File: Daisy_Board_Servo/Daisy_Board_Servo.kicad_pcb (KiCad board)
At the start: 2 copper layers, 29.8 x 46.2 mm, 69 parts, among them IC1 PCA9685PW, IC2 TJA1050T_CM, IC3 LSM6DS3TR-C, IC4 ACS712ELCTR-05B-T, J1 SM04B-SRSS-TB, J10 Conn_01x03_Pin, J11 Conn_01x03_Pin, J12 Conn_01x03_Pin, J13 Conn_01x03_Pin, J14 Conn_01x03_Pin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

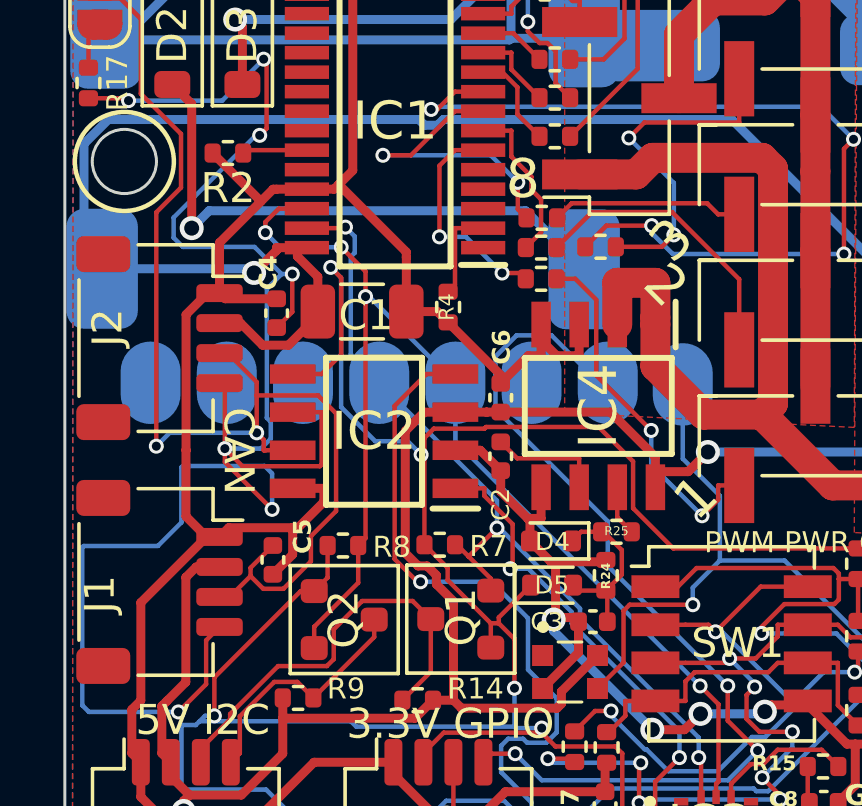
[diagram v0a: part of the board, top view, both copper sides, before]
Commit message: panel updates for lower QTY parts
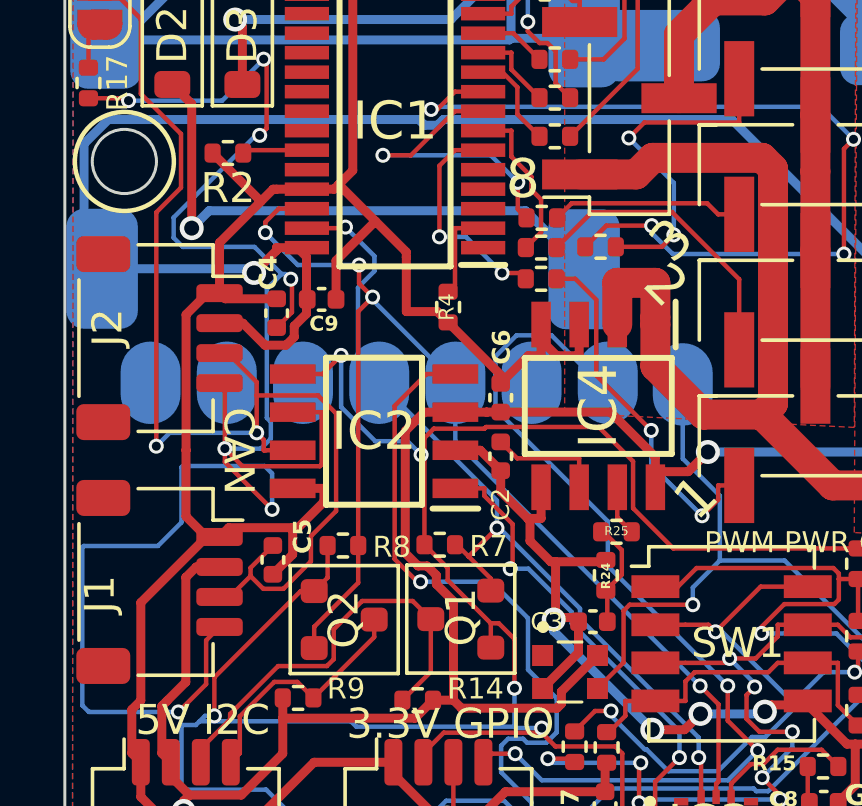
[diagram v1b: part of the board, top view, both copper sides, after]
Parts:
- removed C1: 100nF 50V, Capacitor_SMD:C_1206_3216Metric
- removed D4: ESD9XD, Diode_SMD:D_SOD-523
- removed D5: ESD9X, Diode_SMD:D_SOD-523
- added C9: 100nF 50V, Capacitor_SMD:C_0402_1005Metric, F.Cu at (85.9, 80.0)
- J10, J11, J12, J13, J14, J15, J3, J9: value Conn_01x03_Pin -> X6511WVS-03H-C60D48R2
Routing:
- net +3.3V: track 92.0 -> 84.1 mm
- net GND: track 222.9 -> 226.1 mm
- net Current Sense: track 5.84 -> 3.57 mm
